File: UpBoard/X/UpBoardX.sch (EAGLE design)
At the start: 112 parts, among them CN1 100nF, CN2 100nF, CN3 100nF, CN4 100nF, IC1 SAM3X8E(ARDUINO), Q1 FDS5680, Q2 FDS5680, Q3 FDS5680, Q4 FDS5680

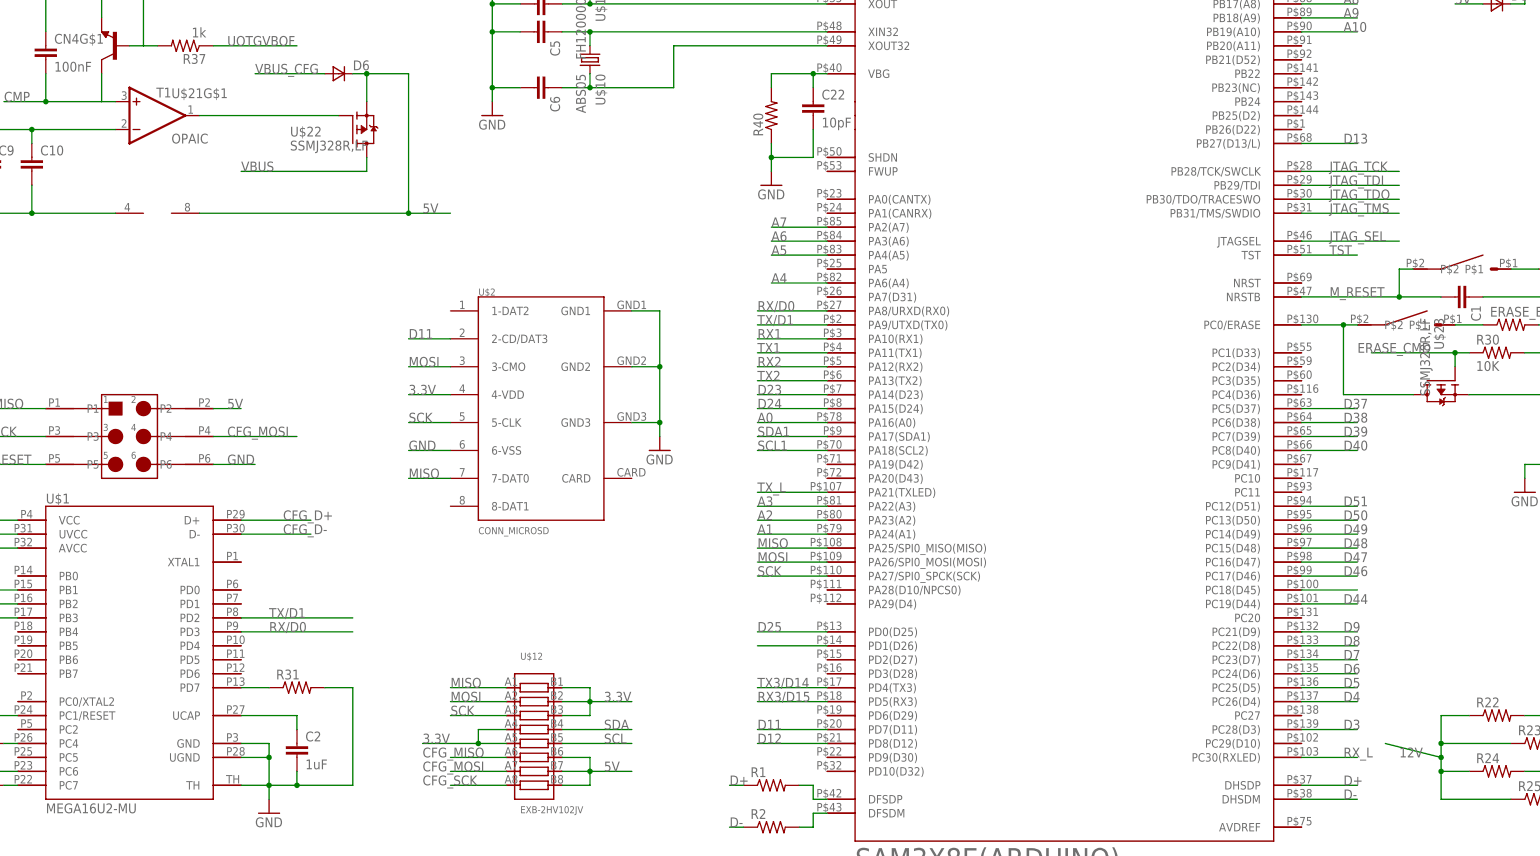
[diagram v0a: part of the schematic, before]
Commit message: Added Patch Circles to highlight areas to be revised
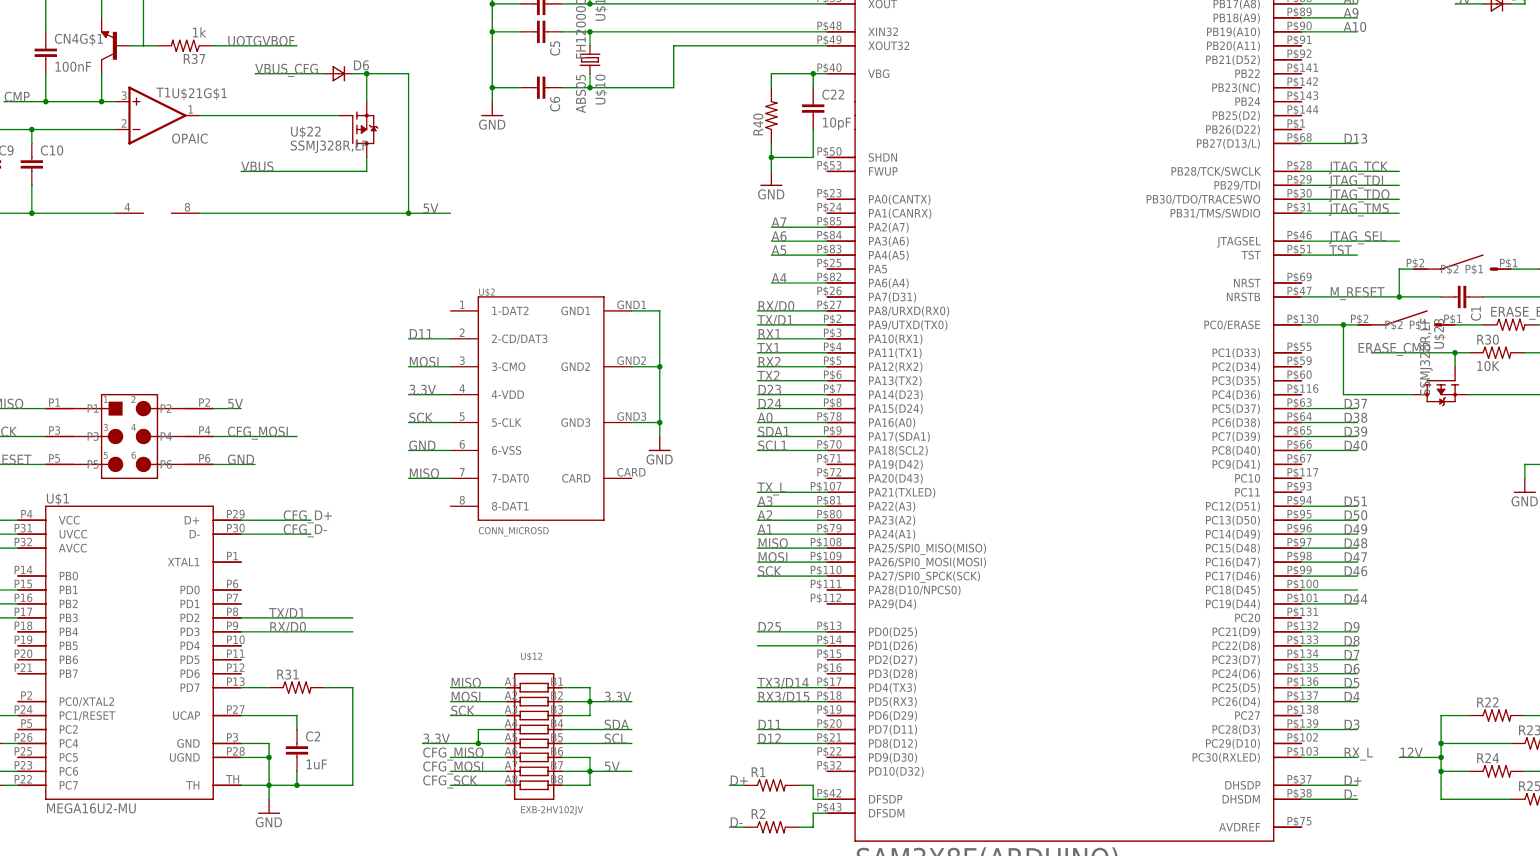
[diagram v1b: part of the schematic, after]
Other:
- note added: "Pull Down Signals"
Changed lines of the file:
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@@
 <text x="53.34" y="205.74" size="10.16" layer="90">UPBOARD X</text>
 <text x="-139.7" y="208.28" size="6.4516" layer="90">SENSOR PACKAGE</text>
+<circle x="-83.82" y="38.1" radius="16.263934375" width="0.1524" layer="101"/>
+<circle x="-121.92" y="66.04" radius="16.06436875" width="0.1524" layer="101"/>
+<circle x="-144.78" y="40.64" radius="7.62" width="0.1524" layer="101"/>
+<circle x="180.34" y="165.1" radius="32.52786875" width="0.1524" layer="101"/>
+<circle x="116.84" y="152.4" radius="19.3440625" width="0.1524" layer="101"/>
+<circle x="-22.86" y="55.88" radius="3.5921" width="0.1524" layer="101"/>
+<circle x="-43.18" y="45.72" radius="44.359190625" width="0.1524" layer="101"/>
+<circle x="-40.64" y="-33.02" radius="5.6796125" width="0.1524" layer="101"/>
+<circle x="297.18" y="-76.2" radius="28.960453125" width="0.1524" layer="101"/>
+<circle x="20.32" y="129.54" radius="11.359225" width="0.1524" layer="101"/>
+<circle x="208.28" y="71.12" radius="22.71845" width="0.1524" layer="101"/>
+<text x="259.08" y="73.66" size="1.778" layer="101">Pull Down Signals</text>
 </plain>
 <instances>
@@
 <pinref part="R25" gate="G$1" pin="1"/>
 <wire x1="177.8" y1="-76.2" x2="190.5" y2="-76.2" width="0.1524" layer="91"/>
-<wire x1="177.8" y1="-68.58" x2="167.64" y2="-66.04" width="0.1524" layer="91"/>
+<wire x1="177.8" y1="-68.58" x2="170.18" y2="-68.58" width="0.1524" layer="91"/>
 <junction x="177.8" y="-68.58"/>
 <label x="170.18" y="-68.58" size="1.778" layer="95"/>
@@
 <wire x1="-76.2" y1="50.8" x2="-83.82" y2="50.8" width="0.1524" layer="91"/>
 <pinref part="CN4" gate="G$1" pin="2"/>
-</segment>
-<segment>
+<junction x="-66.04" y="50.8"/>
+</segment>
+<segment>

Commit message: Revised overly complicated power system
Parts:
- removed R32, R33, R34, R35, R36: VARISTORCN0603, varistor:VARISTORCN0603
- removed RN2: CTS742C083, resistor-net:CTS742C083
- removed T1: (no value), transistor:BC808-NPN-SOT23-BEC
- removed U$14: S10M-TP, UpBoard:S10M-TP
- removed U$21: OPAIC, linear:OPAIC
- removed U$22: SSMJ328R,LF, transistor-fet:SSMJ328R,LF
- added Q7: SSMJ328R,LF, transistor-fet:SSMJ328R,LF
- added R38: (no value), resistor:R-US_R0603
- added RV1, RV2, RV3, RV4, RV5: VARISTORCN0603, varistor:VARISTORCN0603
- added SJ1, SJ2, SJ3, SJ4, SJ5: (no value), jumper:SJ2W
- D6: value (none) -> S10M-TP; device zetex:DSOD323 -> UpBoard:S10M-TP
- R37: value 1k -> (none)
- RN1: value CTS742C083 -> 10K
- RN3: value EXB-2HV102JV -> 1K
- renumbered U$10 to Y2, U$11 to Y1, U$12 to RN3, U$15 to PS2, U$16 to PS1, U$18 to Q6, U$19 to LS1, U$23 to Q5, US1 to PROG, US2 to NATIVE
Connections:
- removed net CMP: CN4G$1.2, RN2.3, RN2.4, T1.C, U$21G$1.+IN
- removed net CMP_GATE: R37.2, RN2.1, T1.B
- removed net N$25: U$21G$1.OUT, U$22.G
- removed net N$31: CN4G$1.1, T1.E
- new net AREF: R37.2, SJ1.3, SJ2.3, SJ3.3, SJ4.3, SJ5.3
- new net AREF0/D51: SJ1.2, U$6.P$16
- new net AREF1/D3: SJ2.2, U$3.13
- new net AREF2/D8: SJ3.2, U$4.13
- new net AREF3/D25: SJ4.2, U$8.13
- new net AREF4/D9: SJ5.2, U$5.7
- new net AVDREF: IC1.AVDREF, R37.1, R38.2
- new net N$5: Q7.S, U$1.UVCC
- net 1.8V: now also CN2G$3.1, CN2G$4.1, CN3G$1.1, CN3G$2.1; no longer CN1G$1.1, CN1G$2.1, CN1G$3.1, CN1G$4.1
- net 12V: now also D6.-; no longer U$14.-
- net 3.3V: now also CN4G$1.1, CN4G$2.1, CN4G$3.1, CN4G$4.1; no longer CN2G$3.1, CN2G$4.1, CN3G$1.1, CN3G$2.1, U$21G$1.-IN
- net 5V: no longer D6.C, U$21G$3.V+, U$22.S
- net BD+: now also RV4.1; no longer R35.1
- net BD-: now also RV5.1; no longer R36.1
- net D+: now also RV1.1; no longer R32.1
- net D-: now also RV2.1; no longer R33.1
- net D25: now also SJ4.1; no longer U$8.13
- net D3: now also SJ2.1; no longer U$3.13
- net D51: now also SJ1.1; no longer U$6.P$16
- net D8: now also SJ3.1; no longer U$4.13
- net D9: now also SJ5.1; no longer U$5.7
- net GND: now also CN1G$2.1, CN1G$3.1, CN1G$4.1, CN4G$1.2, CN4G$2.2, CN4G$3.2, CN4G$4.2, Q7.G, R38.1, RV1.2, RV2.2, RV3.2, RV4.2, RV5.2; no longer CN1G$1.2, CN1G$2.2, CN1G$3.2, CN1G$4.2, CN4G$2.1, CN4G$3.1, CN4G$4.1, R32.2, R33.2, R34.2, R35.2, R36.2, RN2.6, RN2.8, U$21G$3.GND
- net UOTGID: now also RV3.1; no longer R34.1
- net UOTGVBOF: no longer R37.1
- net VBUS: no longer U$22.D
- net VBUS_CFG: now also Q7.D; no longer D6.A, U$1.UVCC
- net VDDANA: now also CN1G$3.2, L2.2; no longer CN4G$3.2, L3.2
- net VDDPLL: now also CN1G$2.2; no longer CN4G$2.2
- net VDDUTMI: now also CN1G$4.2, L3.2; no longer CN4G$4.2, L2.2
- net VIN: now also D6.+; no longer RN2.5, U$14.+
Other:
- moved on the sheet: CN1G$2, CN1G$3, CN1G$4, CN2G$1, CN2G$2, CN2G$3, CN2G$4, CN3G$1, CN3G$2, CN3G$3, CN3G$4, CN4G$1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

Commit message: Simplified power system
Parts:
- removed C20: 10uF, resistor:CPOL-EUA/3216-18R
- removed C22: 10pF, resistor:C-EUC0603
- removed NATIVE, PROG: (no value), adafruit:USBMINIB
- removed Q7: SSMJ328R,LF, transistor-fet:SSMJ328R,LF
- removed R10, R40: (no value), resistor:R-US_R0603
- removed R41, R42: 0R, resistor:R-US_R0402
- removed RN3: 1K, resistor-net:EXB-2HV102JV
- removed U$1: MEGA16U2-MU, atmel:MEGA16U2-MU
- removed U$13: A109214, Cp2:A109214
- removed U$17: 2N7002E, UpBoard B:2N7002E
- removed U$3, U$4: COMS, UpBoard B:15POSD-SUB
- removed U$5: CTRL/PYRO, UpBoard B:9POSD-SUB
- removed U$6: DF12-20PIN_CONNECTOR_HEADER, IMUPACKAGE:DF12-20PIN_CONNECTOR_HEADER
- removed U$7: 2POSTERMINALBLOCK.25"PITCH, terminal_block:2POSTERMINALBLOCK.25"PITCH
- removed U$8: GP, UpBoard B:15POSD-SUB
- added C11: 1uF, resistor:C-EUC0603
- added C15, C16: 10uF, resistor:CPOL-EUA/3216-18R
- added C17: 100uF, resistor:C-EUC0805
- added D9: (no value), zetex:DSOD323
- added IC2: MEGA16U2-MU, atmel:MEGA16U2-MU
- added J1: 2POSTERMINALBLOCK.25"PITCH, terminal_block:2POSTERMINALBLOCK.25"PITCH
- added JP2: A109214, Cp2:A109214
- added Q8: 2N7002E, UpBoard B:2N7002E
- added R$10: 1k, resistor:R-US_R0603
- added R32, R33, R34, R35, R36: (no value), resistor:R-US_R0603
- added R39: 0R, resistor:R-US_R0603
- added RN2: 1K, resistor-net:EXB-2HV102JV
- added US1, US2: (no value), adafruit:USBMINIB
- added X1, X2: COMS, UpBoard B:15POSD-SUB
- added X3: GP, UpBoard B:15POSD-SUB
- added X4: CTRL/PYRO, UpBoard B:9POSD-SUB
- added XA1: DF12-20PIN_CONNECTOR_HEADER, IMUPACKAGE:DF12-20PIN_CONNECTOR_HEADER
- added Y3: 406C35D16M00000, crystal:406C35D16M00000
- C1: value (none) -> 10pF
- C10, C9: value (none) -> 100nF
- C18: value 10uF -> 100uF; device resistor:CPOL-EUA/3216-18R -> resistor:C-EUC0805
- C2: value 1uF -> 22pF
- C3, C4, C5, C6, C7: value (none) -> 22pF
- C8: value (none) -> 10n
- D1: value (none) -> S10M-TP; device zetex:DSOD323 -> UpBoard:S10M-TP
- D6: value S10M-TP -> (none); device UpBoard:S10M-TP -> zetex:DSOD323
- ERASE_EN, RST_EN: value (none) -> 0R
- LS1: value PKMCS0909E4000-R1 -> AI-1440-TWT-24V-2-R; device ATFlightSecretary:PKMCS0909E4000-R1 -> UpBoard:AI-1440-TWT-24V-2-R
- R1, R2: value (none) -> 22
- R11, R12, R13, R14, R9: value (none) -> 1k
- R15: value (none) -> 6.8K
- R16, R17, R18, R20, R21, R22, R23: value (none) -> 10k
- R19: value (none) -> 10K; device resistor:R-US_R0603 -> resistor:R-US_R0402
- R24: value (none) -> 1M
- R26, R29: value 1k -> (none)
- R3, R4: value (none) -> 39
- R30: value 10K -> (none); device resistor:R-US_R0402 -> resistor:R-US_R0603
- R37, R38: value (none) -> 0R; device resistor:R-US_R0603 -> resistor:R-US_R0402
- R5, R6, R7, R8: value (none) -> 65
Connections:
- removed net N$5: Q7.S, U$1.UVCC
- removed net VBUS: NATIVE.VBUS, R26.1
- new net CFG_OSC2: C3.1, IC2.PC0/XTAL2, R24.2, Y3.1
- new net N$3: C2.1, IC2.XTAL1, R24.1, Y3.3
- net 1.8V: now also C15.+; no longer C20.+
- net 12V: now also D1.-, D2.A, R11.1, R12.1, R13.1, R14.1, X1.3, X2.3, X3.3, X4.1, XA1.P$2, XA1.P$3; no longer D5.A, D6.-, R22.1, R23.1, R24.1, R25.1, U$3.3, U$4.3, U$5.1, U$6.P$2, U$6.P$3, U$8.3
- net 3.3V: now also C18.1, C8.1, R19.2, R8.2, RN2.A4, RN2.A5, RN2.B1, RN2.B2, RN2.B3, X1.1, X2.1, X3.1, XA1.P$1; no longer C1.1, C9.1, R30.2, R4.2, RN3.A4, RN3.A5, RN3.B1, RN3.B2, RN3.B3, U$3.1, U$4.1, U$6.P$1, U$8.1
- net 5V: now also C17.1, C9.1, D9.C, R9.1, RN2.B6, RN2.B7, RN2.B8, US1.VBUS; no longer C7.1, C8.1, RN3.B6, RN3.B7, RN3.B8, U$1.AVCC, U$1.VCC, U$13.P2
- net A0: now also X2.14; no longer U$4.14
- net A1: now also X2.15; no longer U$4.15
- net A10: now also R30.1, R36.2; no longer R16.1, R17.2
- net A2: now also X1.14; no longer U$3.14
- net A3: now also X1.15; no longer U$3.15
- net A4: now also X3.14; no longer U$8.14
- net A5: now also X3.15; no longer U$8.15
- net A6: now also R26.1, R32.2; no longer R8.1, R9.2
- net A7: now also R27.1, R33.2; no longer R10.1, R11.2
- net A8: now also R28.1, R34.2; no longer R12.1, R13.2
- net A9: now also R29.1, R35.2; no longer R14.1, R15.2
- net AIN10: now also R30.2, XA1.P$19; no longer R16.2, U$6.P$19
- net AIN6: now also R26.2, X4.8; no longer R8.2, U$5.8
- net AIN7: now also R27.2, X4.9; no longer R10.2, U$5.9
- net AIN8: now also R28.2, XA1.P$17; no longer R12.2, U$6.P$17
- net AIN9: now also R29.2, XA1.P$18; no longer R14.2, U$6.P$18
- net AREF: now also R25.2; no longer R37.2
- net AREF0/D51: now also XA1.P$16; no longer U$6.P$16
- net AREF1/D3: now also X1.13; no longer U$3.13
- net AREF2/D8: now also X2.13; no longer U$4.13
- net AREF3/D25: now also X3.13; no longer U$8.13
- net AREF4/D9: now also X4.7; no longer U$5.7
- net AVDREF: now also R25.1, R31.2; no longer R37.1, R38.2
- net BD+: now also R1.1, US2.D+; no longer PROG.D+, R27.1
- net BD-: now also R2.1, US2.D-; no longer PROG.D-, R28.1
- net CFG_D+: now also IC2.D+, R1.2; no longer R27.2, U$1.D+
- net CFG_D-: now also IC2.D-, R2.2; no longer R28.2, U$1.D-
- net CFG_MISO: now also IC2.PB3, JP2.P1, RN2.A6; no longer RN3.A6, U$1.PB3, U$13.P1
- net CFG_MOSI: now also IC2.PB2, JP2.P4, RN2.A7; no longer RN3.A7, U$1.PB2, U$13.P4
- net CFG_RESET: now also IC2.PC1/RESET, JP2.P5; no longer U$1.PC1/RESET, U$13.P5
- net CFG_SCK: now also IC2.PB1, JP2.P3, RN2.A8; no longer RN3.A8, U$1.PB1, U$13.P3
- net D+: now also R3.1; no longer NATIVE.D+, R1.1
- net D-: now also R4.1, US1.D-; no longer NATIVE.D-, R2.1
- net D12: now also R17.1
- net D13: now also Q8.G, R16.2; no longer U$17.G
- net D23: now also X3.11; no longer U$8.11
- net D24: now also X3.12; no longer U$8.12
- net D37: now also R23.1; no longer R18.1
- net D38: now also R22.1; no longer R19.1
- net D39: now also R21.1; no longer R20.1
- net D40: now also R20.1; no longer R21.1
- net D46: now also XA1.P$11; no longer U$6.P$11
- net D47: now also XA1.P$12; no longer U$6.P$12
- net D48: now also XA1.P$13; no longer U$6.P$13
- net D49: now also XA1.P$14; no longer U$6.P$14
- net D50: now also XA1.P$15; no longer U$6.P$15
- net D6: now also X2.11; no longer U$4.11
- net D7: now also X2.12; no longer U$4.12
- net ERASE_CMD: now also IC2.PC6, R19.1; no longer R30.1, U$1.PC6
- net F0/X+: now also D6.C, R11.2, X4.2; no longer D4.C, R22.2, U$5.2
- net F1/X-: now also D5.C, R12.2, X4.3; no longer D3.C, R23.2, U$5.3
- net F2/Y+: now also D4.C, R13.2, X4.4; no longer D2.C, R24.2, U$5.4
- net F3/Y-: now also D3.C, R14.2, X4.5; no longer D1.C, R25.2, U$5.5
- net GND: now also C1.2, C11.2, C15.-, C16.-, C17.2, C18.2, C3.2, C5.1, D5.A, D6.A, IC2.GND, IC2.TH, IC2.UGND, J1.P$2, JP2.P6, Q8.S, R16.1, R17.2, R22.2, R23.2, R31.1, R32.1, R33.1, R34.1, R35.1, R36.1, R37.2, R38.2, US1.GND, US2.GND, X1.2, X2.2, X3.2, X4.6, XA1.P$20, XA1.P$4, XA1.P$5, Y3.2; no longer C18.-, C20.-, C22.2, C3.1, C5.2, C8.2, D1.A, D2.A, NATIVE.GND, PROG.GND, Q7.G, R11.1, R13.1, R17.1, R19.2, R31.2, R38.1, R40.1, R41.2, R42.2, R9.1, U$1.GND, U$1.TH, U$1.UGND, U$13.P6, U$17.S, U$3.2, U$4.2, U$5.6, U$6.P$20, U$6.P$4, U$6.P$5, U$7.P$2, U$8.2
- net HV: now also R39.2; no longer R3.2
- net JTAG_SEL: now also R38.1; no longer R42.1
- net MISO: now also RN2.A1, X1.6, X2.6, X3.6, XA1.P$6; no longer RN3.A1, U$3.6, U$4.6, U$6.P$6, U$8.6
- net MOSI: now also RN2.A2, X1.7, X2.7, X3.7, XA1.P$7; no longer RN3.A2, U$3.7, U$4.7, U$6.P$7, U$8.7
- net M_RESET: now also C8.2, R$10.1; no longer C1.2, R29.1
- net N$1: now also C11.1, IC2.UCAP; no longer C2.1, U$1.UCAP
- net N$11: now also IC2.PC4, R9.2; no longer R26.2, U$1.PC4
- net N$2: now also R3.2; no longer R1.2
- net N$20: now also IC2.PC7, R$10.2; no longer R29.2, U$1.PC7
- net N$23: now also IC2.PD7, R18.1; no longer R31.1, U$1.PD7
- net N$32: now also C5.2; no longer C4.2
- net N$33: now also LS1.-; no longer LS1.P2
- net N$34: now also C4.2; no longer C3.2
- net N$35: now also C7.1; no longer C6.1
- net N$36: now also C6.1; no longer C5.1
- net N$38: now also Q8.D; no longer U$17.D
- net N$39: now also LS1.+, R39.1; no longer LS1.P1, R3.1
- net N$40: now also R8.1; no longer R4.1
- net N$41: now also C1.1, R15.2; no longer C22.1, R40.2
- net N$42: now also R7.1; no longer R5.1
- net N$44: now also R5.1; no longer R7.1
- net N$7: now also D2.C; no longer D5.C
- net N$9: now also R4.2; no longer R2.2
- net RX/D0: now also IC2.PD3, X3.4; no longer U$1.PD3, U$8.4
- net RX1: now also X1.4; no longer U$3.4
- net RX2: now also X2.4; no longer U$4.4
- net RX3/D15: now also X1.11; no longer U$3.11
- net SCK: now also RN2.A3, X1.8, X2.8, X3.8, XA1.P$8; no longer RN3.A3, U$3.8, U$4.8, U$6.P$8, U$8.8
- net SCL: now also RN2.B5, X1.10, X2.10, X3.10, XA1.P$10; no longer RN3.B5, U$3.10, U$4.10, U$6.P$10, U$8.10
- net SDA: now also RN2.B4, X1.9, X2.9, X3.9, XA1.P$9; no longer RN3.B4, U$3.9, U$4.9, U$6.P$9, U$8.9
- net TST: now also R37.1; no longer R41.1
- net TX/D1: now also IC2.PD2, X3.5; no longer U$1.PD2, U$8.5
- net TX1: now also X1.5; no longer U$3.5
- net TX2: now also X2.5; no longer U$4.5
- net TX3/D14: now also X1.12; no longer U$3.12
- net UOTGID: now also US1.ID; no longer NATIVE.ID
- net VBUS_CFG: now also D9.A, IC2.AVCC, IC2.UVCC, IC2.VCC, JP2.P2, US2.VBUS; no longer PROG.VBUS, Q7.D
- net VDDPLL: now also C16.+; no longer C18.+
- net VIN: now also D1.+, J1.P$1; no longer D6.+, U$7.P$1
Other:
- note removed: "Pull Down Signals"
- moved on the sheet: C1, C10, C2, C3, C4, C5, C6, C7, C8, C9, D2, D3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
